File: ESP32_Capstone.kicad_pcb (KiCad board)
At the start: 4 copper layers, 40.1 x 41.1 mm, 60 parts, among them J1 USB_C_Receptacle_USB2.0_16P, J2 B2B-PH-K-S, J3 Conn_01x03, J4 Conn_01x04, J5 Conn_01x02, SW5 SW_Omron_B3FS, SW6 SW_Omron_B3FS, SW7 SW_Omron_B3FS, U1 ESP32-C3, U2 MCP73831T-2ACI_OT, U4 W25Q32JVSS, Y1 40 MHz

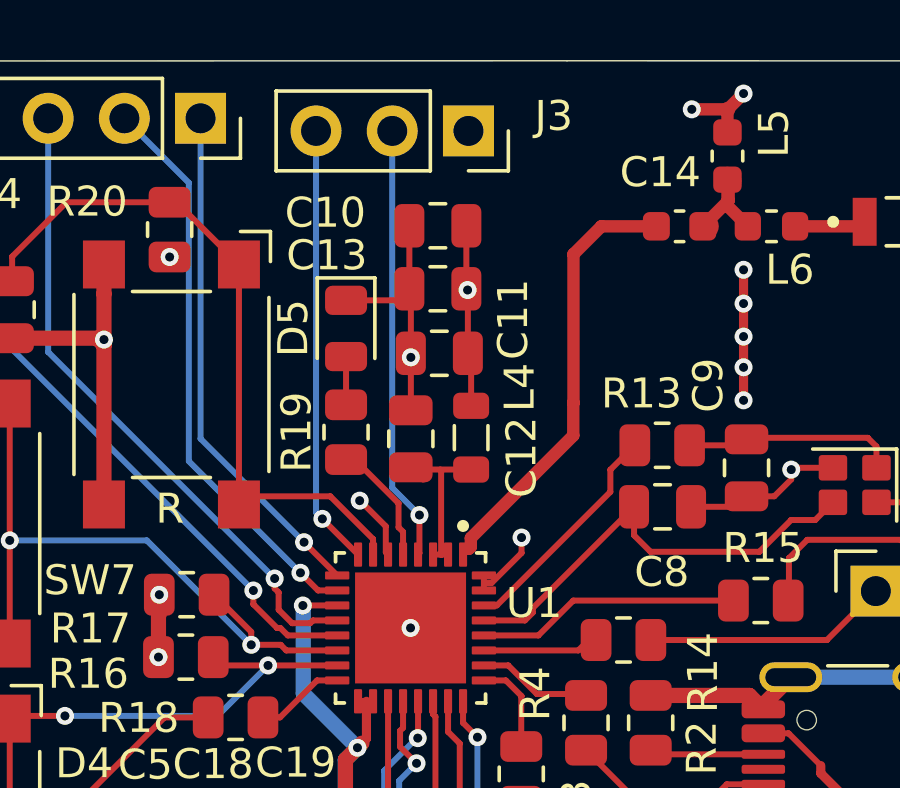
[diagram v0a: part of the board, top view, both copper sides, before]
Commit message: Added a Resistor for GPIO 2, pin 6, as recommended to keep pulled-up
All other information is changed as previous commit; List of numbers on the schematic correspond to the notes from McCreight.
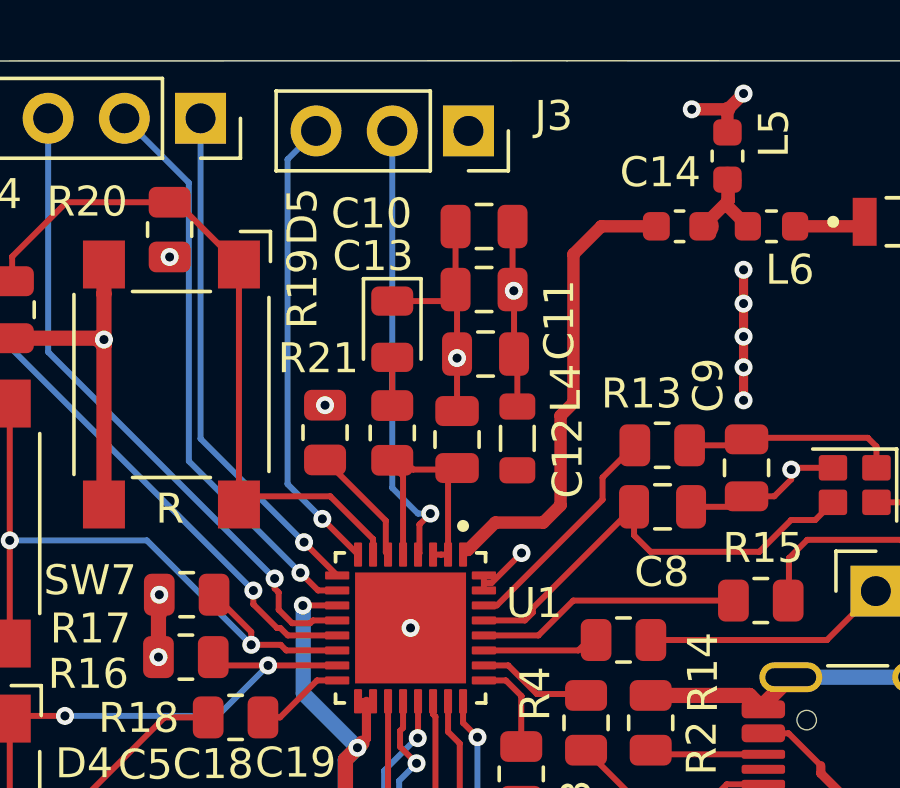
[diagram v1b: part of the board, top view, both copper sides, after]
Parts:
- added R21: 10k, Resistor_SMD:R_0805_2012Metric, F.Cu at (146.3, 98.2)
- R17: value 1k -> 10k
- moved C10 1.54 mm to (151.7, 91.4)
- moved C11 1.54 mm to (151.7, 95.6)
- moved C12 1.54 mm to (150.8, 98.5)
- moved C13 1.54 mm to (151.7, 93.5)
- moved D5 1.54 mm to (148.6, 94.8)
- moved L4 1.54 mm to (152.8, 98.4)
- moved R19 1.54 mm to (148.6, 98.2)
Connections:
- U1 pad 6: +3.3V -> Net-(U1-GPIO2)
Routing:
- net Net-(U1-GPIO2): track 0.00 -> 4.02 mm
- net +3.3V: track 67.4 -> 64.7 mm
- net Net-(U1-LNA_IN): track 14.7 -> 15.7 mm
- net SENSOR_OUT: track 14.7 -> 15.5 mm
- net GPIO_PWR: track 14.4 -> 14.9 mm
- net Net-(U1-XTAL_32K_N): track 4.13 -> 3.58 mm
